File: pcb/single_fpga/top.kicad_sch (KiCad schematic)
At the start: 0 parts

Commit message: Updated.
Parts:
- added C13: 100uF, Capacitor_SMD:CP_Elec_10x10, symbol Device:C
- added C15: .1uF, Capacitor_SMD:C_0603_1608Metric, symbol Device:C
- added C16, C17: 1uF, Capacitor_SMD:C_1206_3216Metric, symbol Device:C
- added J13: Main Power Input, Connector_JST:JST_XH_B2B-XH-A_1x02_P2.50mm_Vertical, symbol Connector_Generic:Conn_01x02
- added VR5: MCP1700T-3302E/TT, Package_TO_SOT_SMD:SOT-23, symbol Regulator_Linear:MCP1700x-330xxTT
- added Y1: (no value), multi_fpga:ECS-TXO-5032-122.8-TR, symbol multi_fpga:TCXO_OSC
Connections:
- new net +3V3: C15.1, C17.1, VR5.2 (VO), Y1.4 (VDD)
- new net +5V: C13.1, C16.1, J13.1 (Pin_1), VR5.3 (VI)
- new net GND: C13.2, C15.2, C16.2, C17.2, J13.2 (Pin_2), VR5.1 (GND), Y1.2 (GND)
- new net TCXO_CLK: Y1.3 (OUTPUT)
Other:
- added sheet AC7200 FPGA Module (ac7200_mod.kicad_sch)

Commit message: Added AC7200 connector group. Placed mics and caps. Added mounting holes and camera holes.
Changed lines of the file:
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@@
 	)
 	(sheet
-		(at 64.77 104.14)
+		(at 63.5 109.22)
 		(size 39.37 17.78)
 		(exclude_from_sim no)
@@
 		)
 		(property "Sheetname" "AC7200 FPGA Module"
-			(at 64.77 103.4284 0)
+			(at 63.5 108.5084 0)
 			(show_name no)
 			(do_not_autoplace no)
@@
 		)
 		(property "Sheetfile" "ac7200_mod.kicad_sch"
-			(at 64.77 122.5046 0)
+			(at 63.5 127.5846 0)
 			(show_name no)
 			(do_not_autoplace no)

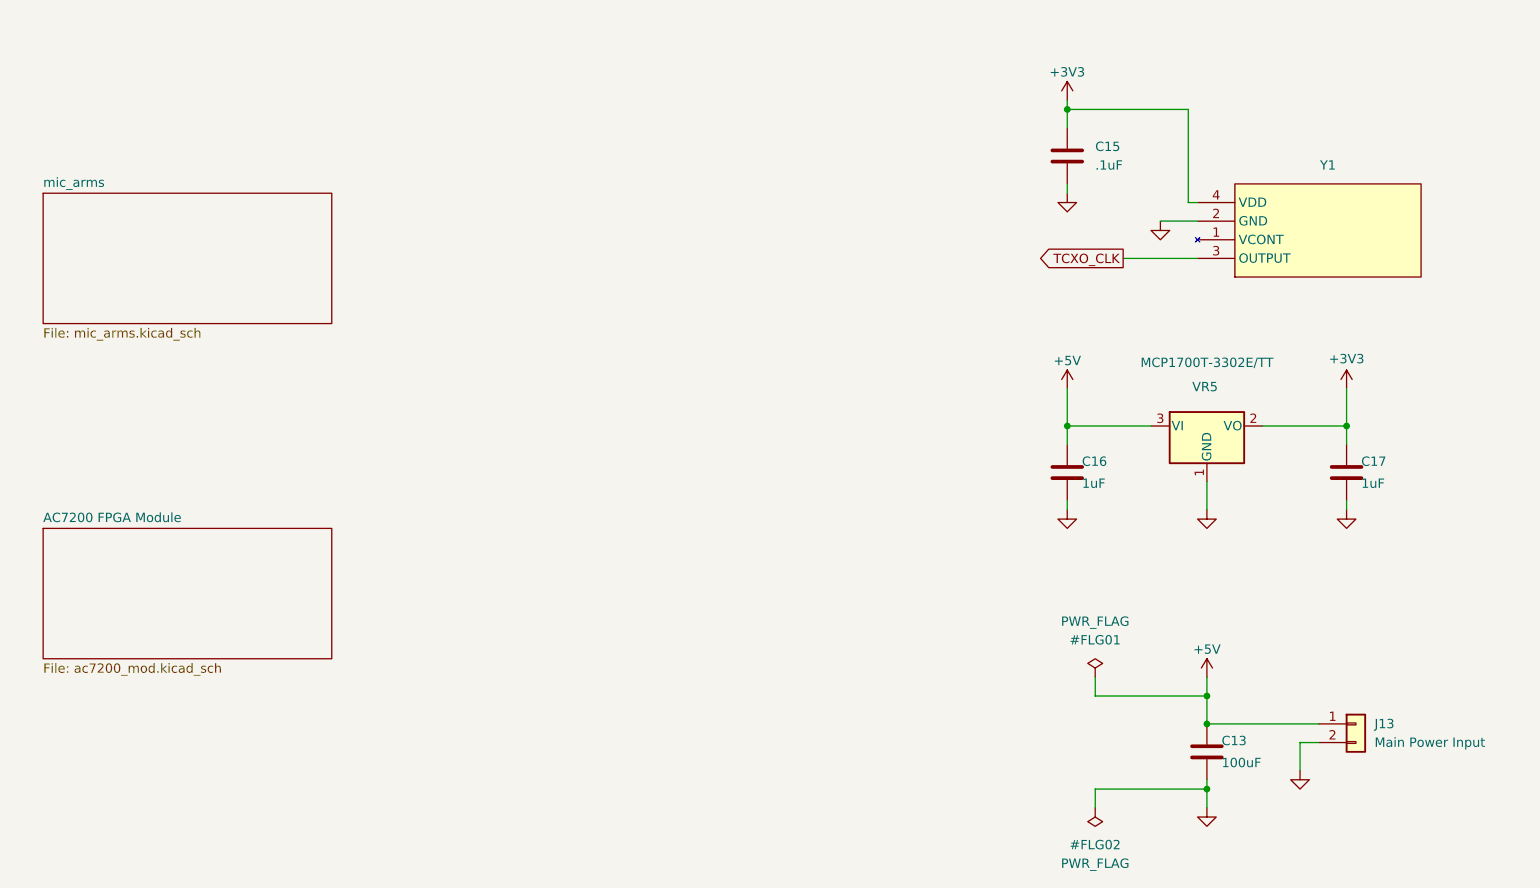
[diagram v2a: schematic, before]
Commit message: Added new regulators. Added clock drivers.
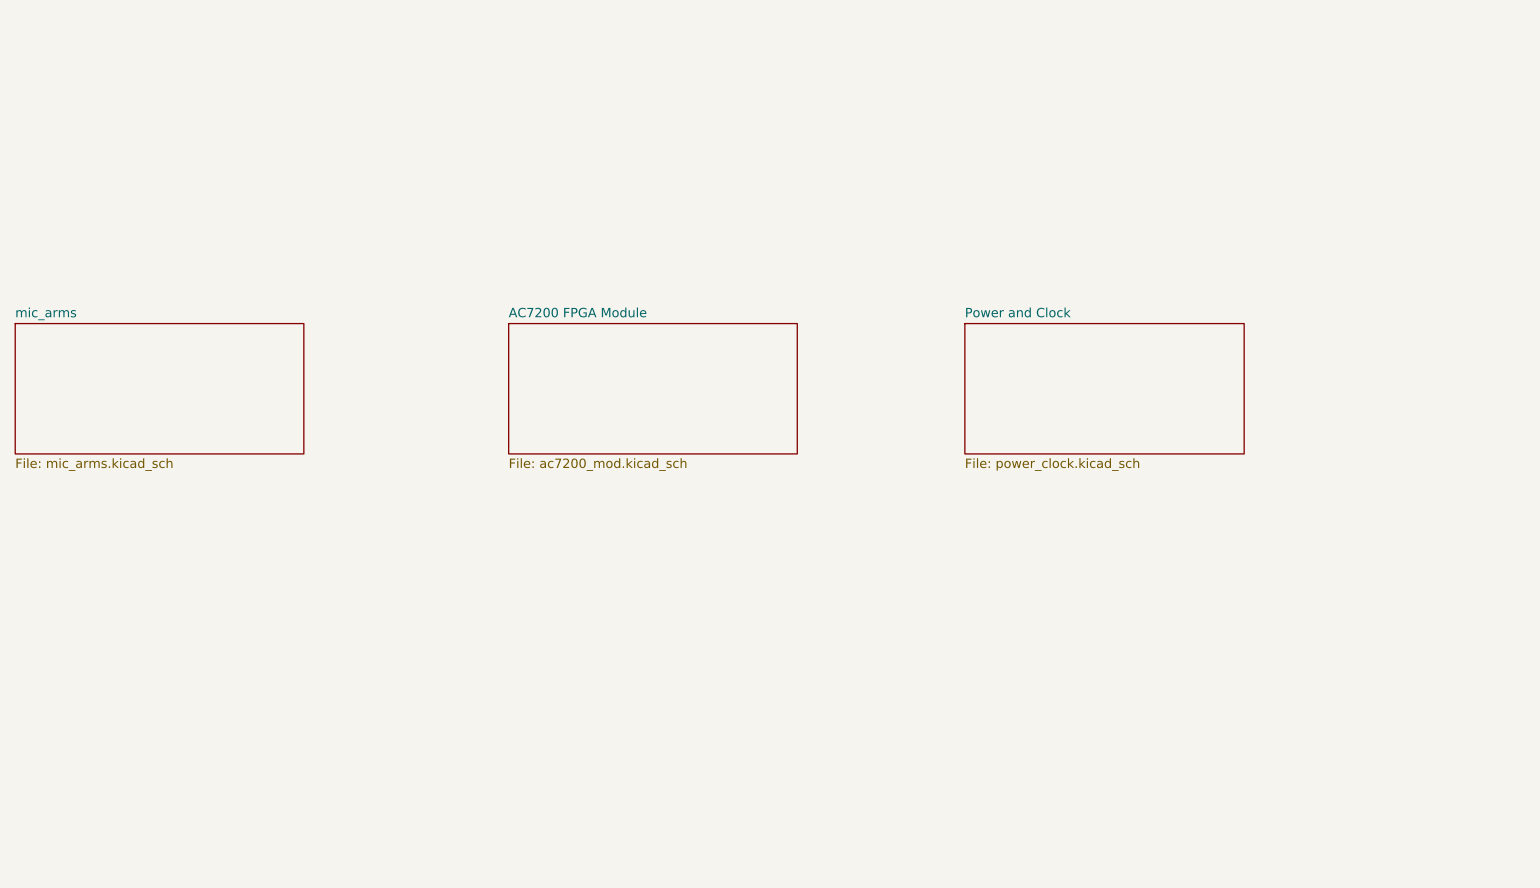
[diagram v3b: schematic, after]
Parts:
- removed C13: 100uF, Capacitor_SMD:CP_Elec_10x10, symbol Device:C
- removed C15: .1uF, Capacitor_SMD:C_0603_1608Metric, symbol Device:C
- removed C16, C17: 1uF, Capacitor_SMD:C_1206_3216Metric, symbol Device:C
- removed J13: Main Power Input, Connector_JST:JST_XH_B2B-XH-A_1x02_P2.50mm_Vertical, symbol Connector_Generic:Conn_01x02
- removed VR5: MCP1700T-3302E/TT, Package_TO_SOT_SMD:SOT-23, symbol Regulator_Linear:MCP1700x-330xxTT
- removed Y1: (no value), multi_fpga:ECS-TXO-5032-122.8-TR, symbol multi_fpga:TCXO_OSC
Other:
- added sheet Power and Clock (power_clock.kicad_sch)

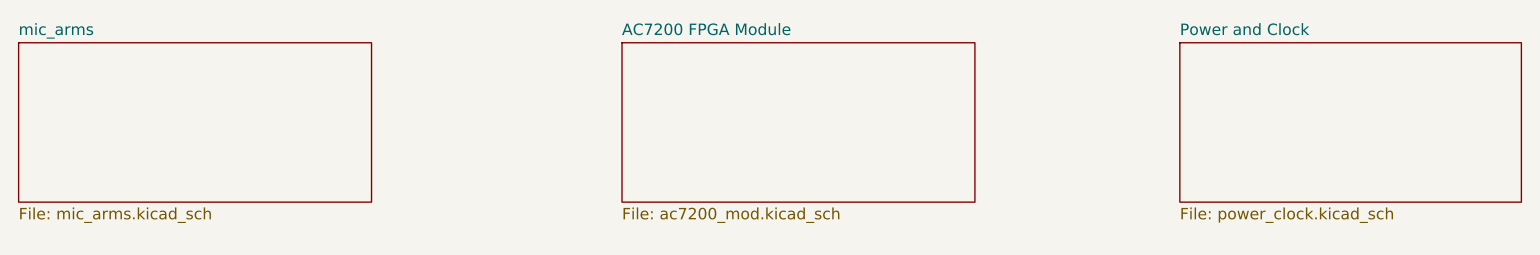
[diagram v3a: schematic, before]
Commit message: Reorganized sheets for two-boards. Fixed connector off-grid problems.
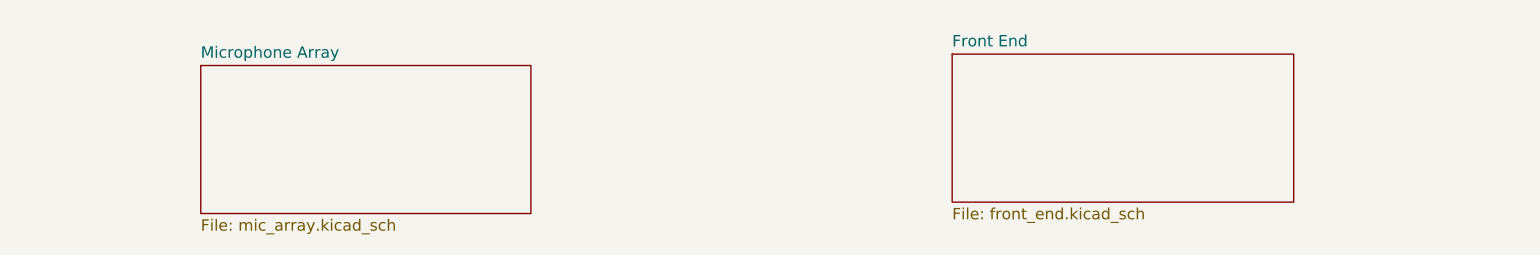
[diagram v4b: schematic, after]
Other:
- removed sheet AC7200 FPGA Module
- removed sheet Power and Clock
- removed sheet mic_arms
- added sheet Front End (front_end.kicad_sch)
- added sheet Microphone Array (mic_array.kicad_sch)
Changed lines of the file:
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@@
 	(paper "A4")
 	(sheet
-		(at 59.69 81.28)
-		(size 39.37 17.78)
+		(at 80.01 83.82)
+		(size 36.83 16.51)
 		(exclude_from_sim no)
 		(in_bom yes)
@@
 			(color 0 0 0 0)
 		)
-		(property "Sheetname" "mic_arms"
-			(at 59.69 80.5684 0)
+		(property "Sheetname" "Microphone Array"
+			(at 80.01 83.1084 0)
 			(show_name no)
 			(do_not_autoplace no)
@@
 			)
 		)
-		(property "Sheetfile" "mic_arms.kicad_sch"
-			(at 59.69 99.6446 0)
+		(property "Sheetfile" "mic_array.kicad_sch"
+			(at 80.01 100.9146 0)
 			(show_name no)
 			(do_not_autoplace no)
@@
 			(project "top"
 				(path "/12638caa-1907-413e-8e98-06abbbf6ccbc"
-					(page "2")
+					(page "21")
 				)
 			)
@@
 	)
 	(sheet
-		(at 189.23 81.28)
-		(size 38.1 17.78)
+		(at 163.83 82.55)
+		(size 38.1 16.51)
 		(exclude_from_sim no)
 		(in_bom yes)
@@
 			(color 0 0 0 0)
 		)
-		(property "Sheetname" "Power and Clock"
-			(at 189.23 80.5684 0)
+		(property "Sheetname" "Front End"
+			(at 163.83 81.8384 0)
 			(show_name no)
 			(do_not_autoplace no)
@@
 			)
 		)
-		(property "Sheetfile" "power_clock.kicad_sch"
-			(at 189.23 99.6446 0)
+		(property "Sheetfile" "front_end.kicad_sch"
+			(at 163.83 99.6446 0)
 			(show_name no)
 			(do_not_autoplace no)
@@
 			(project "top"
 				(path "/12638caa-1907-413e-8e98-06abbbf6ccbc"
-					(page "20")
+					(page "22")
 				)
 			)
-		)
-	)
-	(sheet
-		(at 127 81.28)
-		(size 39.37 17.78)
-		(exclude_from_sim no)
-		(in_bom yes)
-		(on_board yes)
-		(dnp no)
-		(fields_autoplaced yes)
-		(stroke
-			(width 0.1524)
-			(type solid)
-		)
-		(fill
-			(color 0 0 0 0)
-		)
-		(property "Sheetname" "AC7200 FPGA Module"
-			(at 127 80.5684 0)
-			(show_name no)
-			(do_not_autoplace no)
-			(effects
-				(font
-					(size 1.27 1.27)
-				)
-				(justify left bottom)
-			)
-		)
-		(property "Sheetfile" "ac7200_mod.kicad_sch"
-			(at 127 99.6446 0)
-			(show_name no)
-			(do_not_autoplace no)
-			(effects
-				(font
-					(size 1.27 1.27)
-				)
-				(justify left top)
-			)
-		)
-		(instances
-			(project "top"
-				(path "/12638caa-1907-413e-8e98-06abbbf6ccbc"
-					(page "15")
-				)
-			)
